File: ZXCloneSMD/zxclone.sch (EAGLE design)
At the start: 21 parts, among them IC1 TLC272D

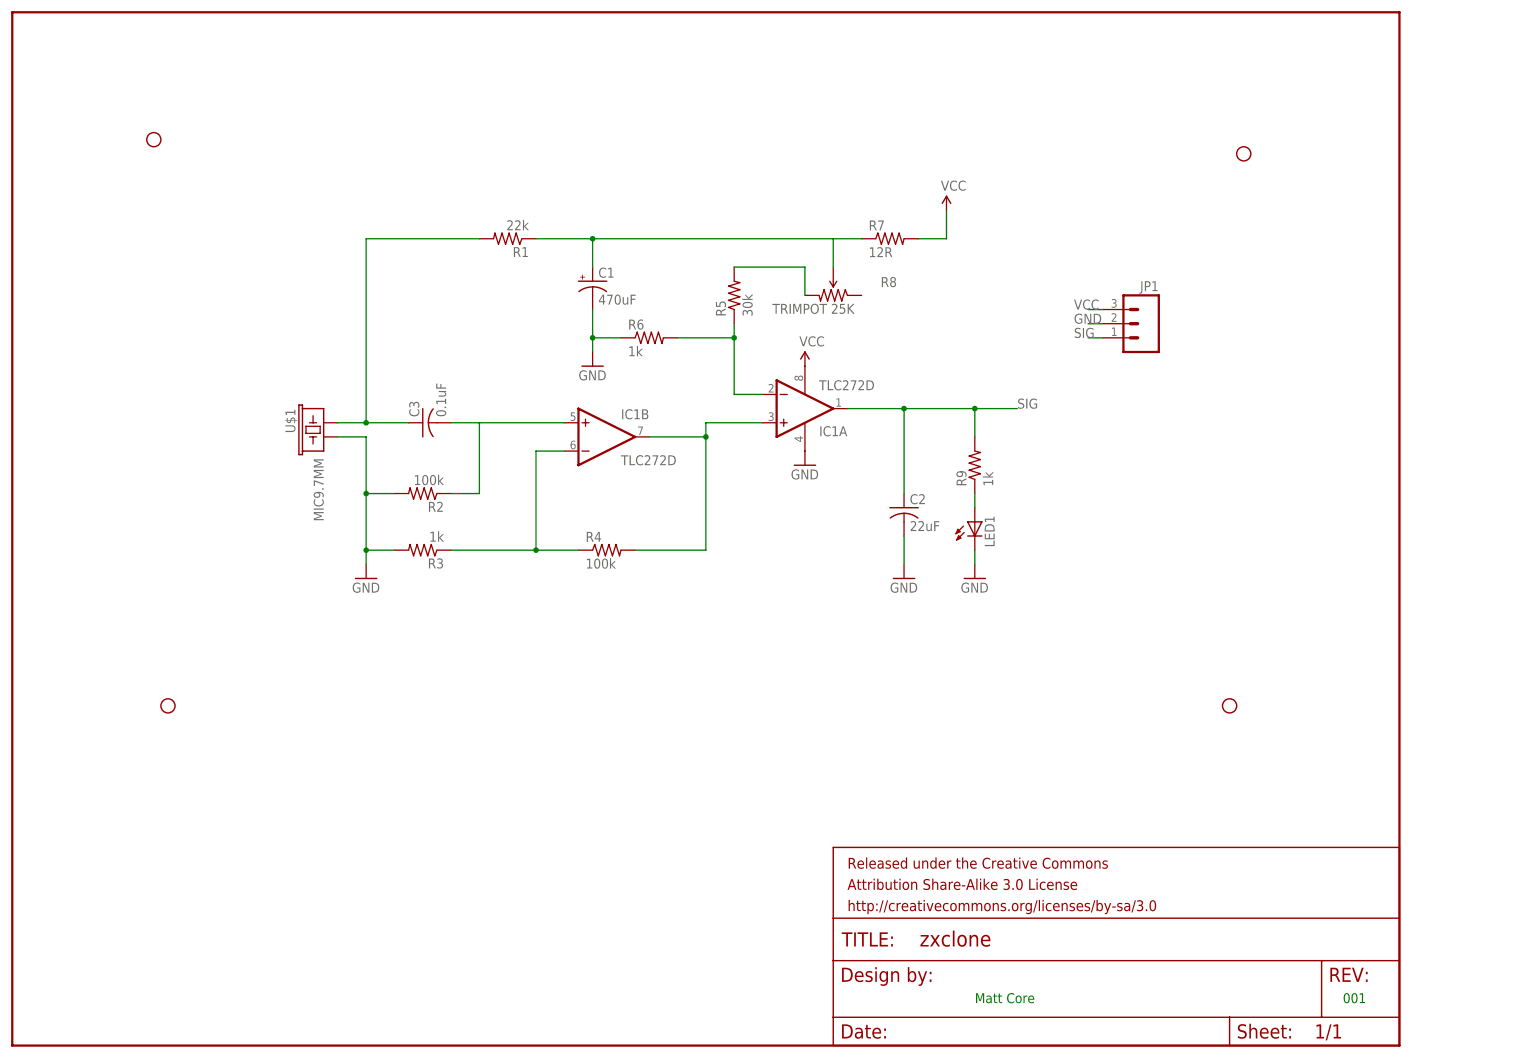
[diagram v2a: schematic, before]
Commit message: Early revision (not yet final) of XBee therm board
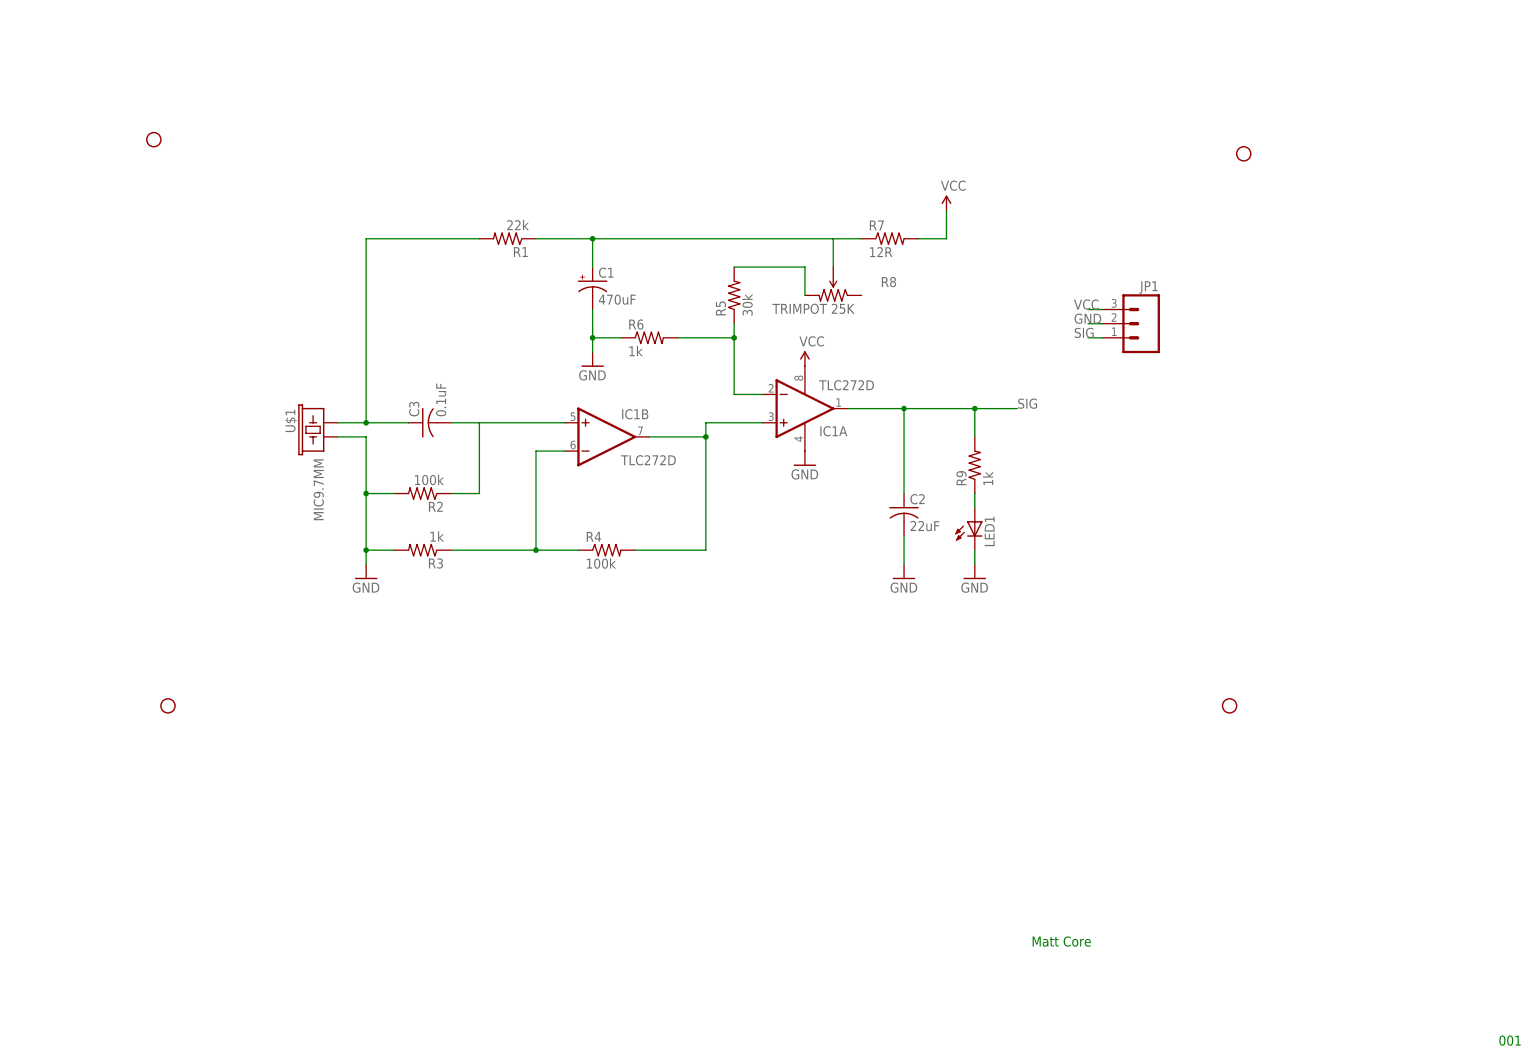
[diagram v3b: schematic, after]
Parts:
- removed FRAME1: FRAME-LETTER, SparkFun-Aesthetics:FRAME-LETTER
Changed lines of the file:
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@@
 <grid distance="0.1" unitdist="inch" unit="inch" style="lines" multiple="1" display="no" altdistance="0.01" altunitdist="inch" altunit="inch"/>
 <layers>
-<layer number="1" name="Top" color="4" fill="1" visible="yes" active="no"/>
-<layer number="16" name="Bottom" color="1" fill="1" visible="yes" active="no"/>
-<layer number="17" name="Pads" color="2" fill="1" visible="yes" active="no"/>
-<layer number="18" name="Vias" color="2" fill="1" visible="yes" active="no"/>
-<layer number="19" name="Unrouted" color="6" fill="1" visible="yes" active="no"/>
-<layer number="20" name="Dimension" color="15" fill="1" visible="yes" active="no"/>
-<layer number="21" name="tPlace" color="16" fill="1" visible="yes" active="no"/>
-<layer number="22" name="bPlace" color="14" fill="1" visible="yes" active="no"/>
-<layer number="23" name="tOrigins" color="15" fill="1" visible="yes" active="no"/>
-<layer number="24" name="bOrigins" color="15" fill="1" visible="yes" active="no"/>
-<layer number="25" name="tNames" color="7" fill="1" visible="yes" active="no"/>
-<layer number="26" name="bNames" color="7" fill="1" visible="yes" active="no"/>
-<layer number="27" name="tValues" color="7" fill="1" visible="yes" active="no"/>
-<layer number="28" name="bValues" color="7" fill="1" visible="yes" active="no"/>
+<layer number="1" name="Top" color="4" fill="1" visible="no" active="no"/>
+<layer number="16" name="Bottom" color="1" fill="1" visible="no" active="no"/>
+<layer number="17" name="Pads" color="2" fill="1" visible="no" active="no"/>
+<layer number="18" name="Vias" color="2" fill="1" visible="no" active="no"/>
+<layer number="19" name="Unrouted" color="6" fill="1" visible="no" active="no"/>
+<layer number="20" name="Dimension" color="15" fill="1" visible="no" active="no"/>
+<layer number="21" name="tPlace" color="16" fill="1" visible="no" active="no"/>
+<layer number="22" name="bPlace" color="14" fill="1" visible="no" active="no"/>
+<layer number="23" name="tOrigins" color="15" fill="1" visible="no" active="no"/>
+<layer number="24" name="bOrigins" color="15" fill="1" visible="no" active="no"/>
+<layer number="25" name="tNames" color="7" fill="1" visible="no" active="no"/>
+<layer number="26" name="bNames" color="7" fill="1" visible="no" active="no"/>
+<layer number="27" name="tValues" color="7" fill="1" visible="no" active="no"/>
+<layer number="28" name="bValues" color="7" fill="1" visible="no" active="no"/>
 <layer number="29" name="tStop" color="7" fill="3" visible="no" active="no"/>
 <layer number="30" name="bStop" color="7" fill="6" visible="no" active="no"/>
@@
 <layer number="35" name="tGlue" color="7" fill="4" visible="no" active="no"/>
 <layer number="36" name="bGlue" color="7" fill="5" visible="no" active="no"/>
-<layer number="37" name="tTest" color="7" fill="1" visible="yes" active="no"/>
-<layer number="38" name="bTest" color="7" fill="1" visible="yes" active="no"/>
+<layer number="37" name="tTest" color="7" fill="1" visible="no" active="no"/>
+<layer number="38" name="bTest" color="7" fill="1" visible="no" active="no"/>
 <layer number="39" name="tKeepout" color="4" fill="11" visible="no" active="no"/>
 <layer number="40" name="bKeepout" color="1" fill="11" visible="no" active="no"/>
@@
 <layer number="44" name="Drills" color="7" fill="1" visible="no" active="no"/>
 <layer number="45" name="Holes" color="7" fill="1" visible="no" active="no"/>
-<layer number="46" name="Milling" color="3" fill="1" visible="yes" active="no"/>
-<layer number="47" name="Measures" color="7" fill="1" visible="yes" active="no"/>
-<layer number="48" name="Document" color="7" fill="1" visible="yes" active="no"/>
-<layer number="49" name="Reference" color="7" fill="1" visible="yes" active="no"/>
-<layer number="50" name="dxf" color="7" fill="1" visible="yes" active="no"/>
-<layer number="51" name="tDocu" color="6" fill="1" visible="yes" active="no"/>
-<layer number="52" name="bDocu" color="7" fill="1" visible="yes" active="no"/>
-<layer number="53" name="tGND_GNDA" color="7" fill="9" visible="yes" active="no"/>
-<layer number="54" name="bGND_GNDA" color="1" fill="9" visible="yes" active="no"/>
-<layer number="56" name="wert" color="7" fill="1" visible="yes" active="no"/>
+<layer number="46" name="Milling" color="3" fill="1" visible="no" active="no"/>
+<layer number="47" name="Measures" color="7" fill="1" visible="no" active="no"/>
+<layer number="48" name="Document" color="7" fill="1" visible="no" active="no"/>
+<layer number="49" name="Reference" color="7" fill="1" visible="no" active="no"/>
+<layer number="50" name="dxf" color="7" fill="1" visible="no" active="no"/>
+<layer number="51" name="tDocu" color="6" fill="1" visible="no" active="no"/>
+<layer number="52" name="bDocu" color="7" fill="1" visible="no" active="no"/>
+<layer number="53" name="tGND_GNDA" color="7" fill="9" visible="no" active="no"/>
+<layer number="54" name="bGND_GNDA" color="1" fill="9" visible="no" active="no"/>
+<layer number="56" name="wert" color="7" fill="1" visible="no" active="no"/>
 <layer number="91" name="Nets" color="2" fill="1" visible="yes" active="yes"/>
 <layer number="92" name="Busses" color="1" fill="1" visible="yes" active="yes"/>
@@
 <part name="C1" library="resistor" deviceset="CPOL-US" device="E2.5-7" value="470uF"/>
 <part name="U$1" library="SparkFun-Sensors" deviceset="MIC" device="9.7MM"/>
-<part name="FRAME1" library="SparkFun-Aesthetics" deviceset="FRAME-LETTER" device=""/>
 <part name="GND1" library="SparkFun-Aesthetics" deviceset="GND" device=""/>
 <part name="SUPPLY1" library="SparkFun-Aesthetics" deviceset="VCC" device=""/>
@@
 <part name="LED1" library="led" deviceset="LED" device="SML0603"/>
 <part name="GND5" library="SparkFun-Aesthetics" deviceset="GND" device=""/>
+<part name="FRAME1" library="frames" deviceset="FRAME_A_L" device=""/>
 </parts>
 <sheets>
 <sheet>
 <plain>
-<text x="170.18" y="15.24" size="1.778" layer="91">Matt Core</text>
-<text x="236.22" y="15.24" size="1.778" layer="91">001</text>
+<text x="180.34" y="25.4" size="1.778" layer="91">Matt Core</text>
+<text x="264.16" y="7.62" size="1.778" layer="91">001</text>
 </plain>
 <instances>
@@
 <instance part="C1" gate="G$1" x="101.6" y="144.78"/>
 <instance part="U$1" gate="G$1" x="53.34" y="119.38" rot="MR270"/>
-<instance part="FRAME1" gate="G$1" x="-2.54" y="7.62"/>
-<instance part="FRAME1" gate="G$2" x="144.78" y="7.62"/>
 <instance part="GND1" gate="1" x="101.6" y="129.54"/>
 <instance part="SUPPLY1" gate="1" x="165.1" y="157.48"/>
@@
 <instance part="LED1" gate="G$1" x="170.18" y="101.6"/>
 <instance part="GND5" gate="1" x="170.18" y="91.44"/>
+<instance part="FRAME1" gate="G$1" x="0" y="0"/>
+<instance part="FRAME1" gate="G$2" x="172.72" y="0"/>
 </instances>
 <busses>
